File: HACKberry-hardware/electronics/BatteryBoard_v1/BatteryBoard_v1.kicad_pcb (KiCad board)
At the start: 2 copper layers, 8 x 18.1 mm, 0 parts

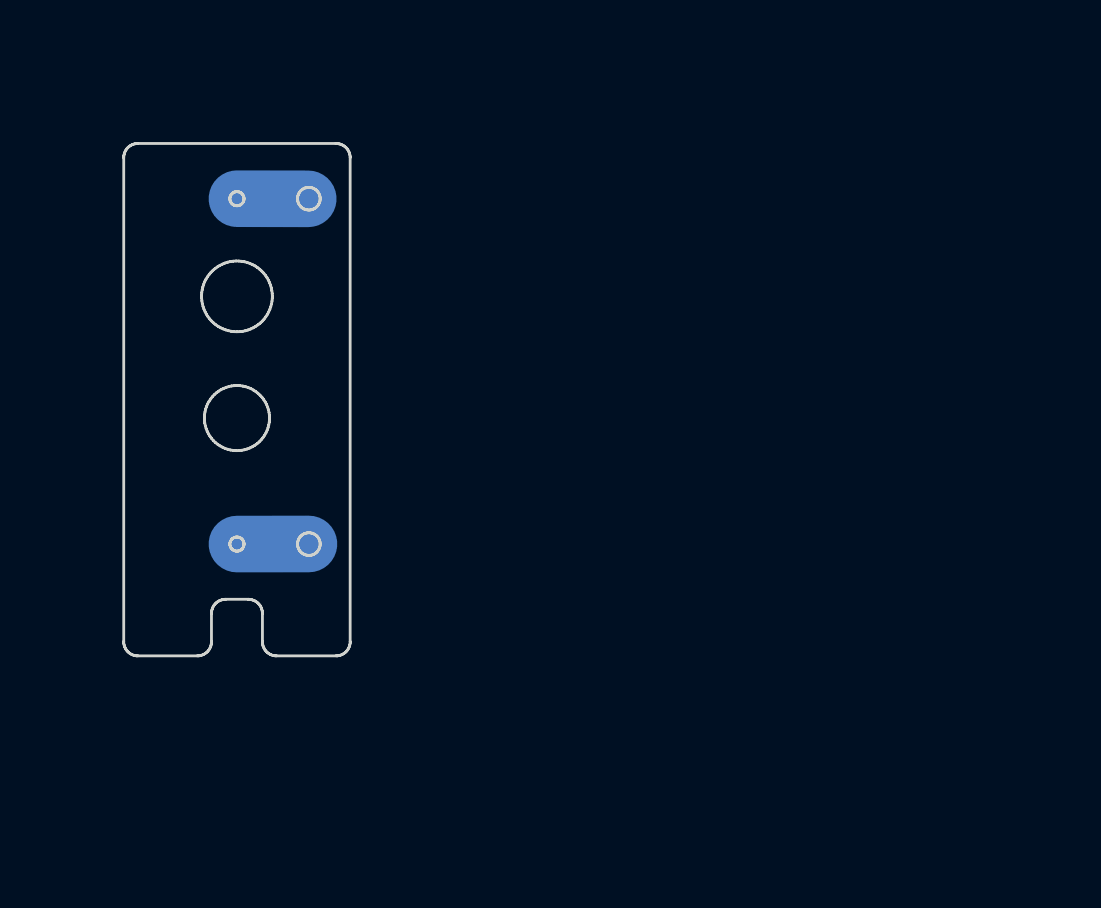
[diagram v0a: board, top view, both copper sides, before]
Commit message: Updated the HandBoard
changed the voltage for sensor from 3.3[V] to 5.0[V].
modified the garber data for milling.
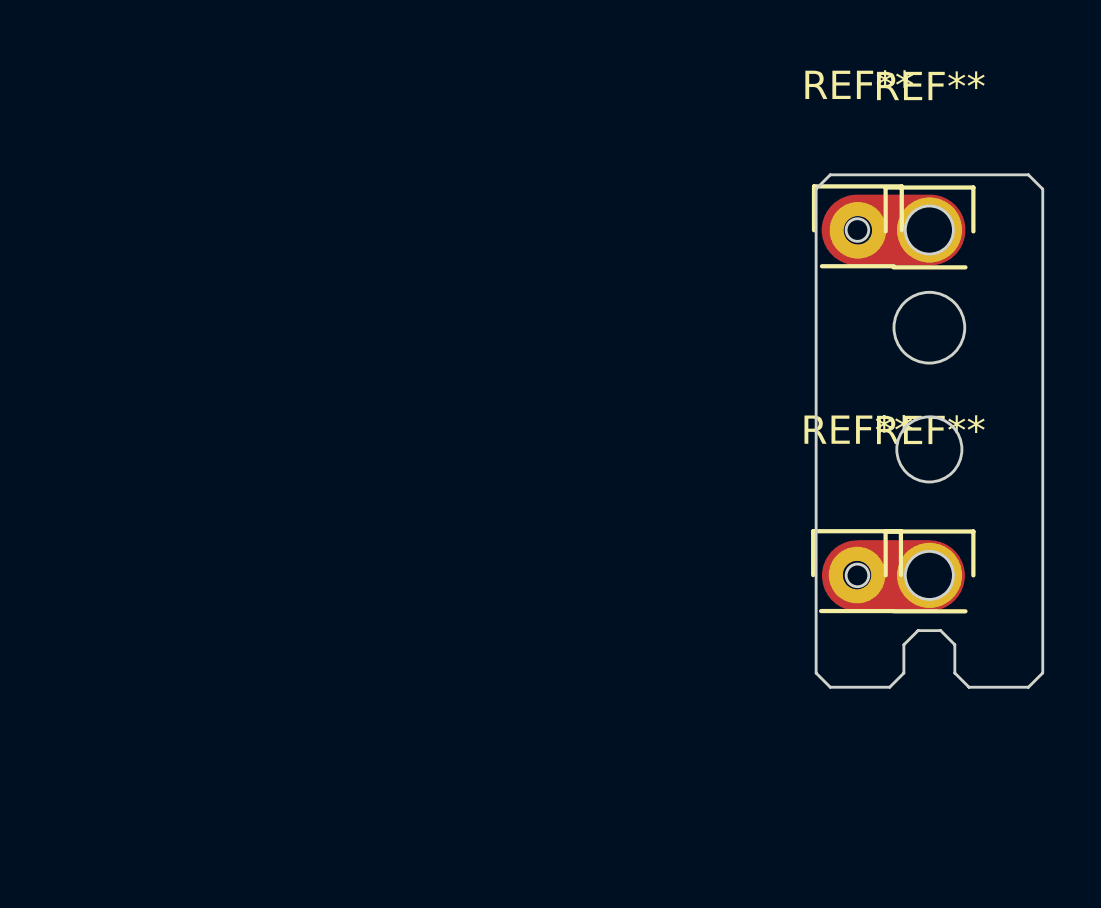
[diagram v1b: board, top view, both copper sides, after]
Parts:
- added REF**: Pin_Header_Straight_1x01, Pin_Headers:Pin_Header_Straight_1x01, F.Cu at (228.2, 136.6)
- added REF**: Pin_Header_Straight_1x01, Pin_Headers:Pin_Header_Straight_1x01, F.Cu at (230.8, 136.7)
- added REF**: Pin_Header_Straight_1x01, Pin_Headers:Pin_Header_Straight_1x01, F.Cu at (228.2, 148.8)
- added REF**: Pin_Header_Straight_1x01, Pin_Headers:Pin_Header_Straight_1x01, F.Cu at (230.8, 148.8)
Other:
- outline, holes or cut-outs redrawn

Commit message: Uploaded the PCB files for manufacturing
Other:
- outline, holes or cut-outs redrawn
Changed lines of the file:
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@@
     (area 218.156713 130.341 240.803287 152.811101)
     (thickness 1.6)
-    (drawings 22)
+    (drawings 20)
     (tracks 4)
     (zones 0)
@@
   (layers
     (0 F.Cu signal)
-    (31 B.Cu signal hide)
-    (32 B.Adhes user hide)
-    (33 F.Adhes user hide)
-    (34 B.Paste user hide)
-    (35 F.Paste user hide)
-    (36 B.SilkS user hide)
-    (37 F.SilkS user hide)
-    (38 B.Mask user hide)
-    (39 F.Mask user hide)
-    (40 Dwgs.User user hide)
-    (41 Cmts.User user hide)
-    (42 Eco1.User user hide)
-    (43 Eco2.User user hide)
+    (31 B.Cu signal)
+    (32 B.Adhes user)
+    (33 F.Adhes user)
+    (34 B.Paste user)
+    (35 F.Paste user)
+    (36 B.SilkS user)
+    (37 F.SilkS user)
+    (38 B.Mask user)
+    (39 F.Mask user)
+    (40 Dwgs.User user)
+    (41 Cmts.User user)
+    (42 Eco1.User user)
+    (43 Eco2.User user)
     (44 Edge.Cuts user)
   )
   (setup
-    (last_trace_width 2.5)
+    (last_trace_width 0.254)
     (user_trace_width 2)
     (user_trace_width 2.5)
@@
     (mod_text_width 0.15)
     (pad_size 2.3 2.3)
-    (pad_drill 1.7)
+    (pad_drill 1.5)
     (pad_to_mask_clearance 0.2)
     (aux_axis_origin 0 0)
@@
       (drillshape 0)
       (scaleselection 1)
-      (outputdirectory 151101BatteryBoard_v1_01/))
+      (outputdirectory 151112BatteryBoard_v1_01/))
   )
   (net 0 "")
@@
     (fp_line (start -1.55 -1.55) (end 1.55 -1.55) (layer F.SilkS) (width 0.15))
     (fp_line (start -1.27 1.27) (end 1.27 1.27) (layer F.SilkS) (width 0.15))
-    (pad 1 thru_hole circle (at 0 -0.05) (size 2.3 2.3) (drill 1.7) (layers *.Cu *.Mask F.SilkS))
+    (pad 1 thru_hole circle (at 0 -0.05) (size 2.3 2.3) (drill 1.5) (layers *.Cu *.Mask F.SilkS))
     (model Pin_Headers.3dshapes/Pin_Header_Straight_1x01.wrl
       (at (xyz 0 0 0))
@@
     (fp_line (start -1.55 -1.55) (end 1.55 -1.55) (layer F.SilkS) (width 0.15))
     (fp_line (start -1.27 1.27) (end 1.27 1.27) (layer F.SilkS) (width 0.15))
-    (pad 1 thru_hole circle (at 0 0) (size 2.3 2.3) (drill 1.7) (layers *.Cu *.Mask F.SilkS))
+    (pad 1 thru_hole circle (at 0 0) (size 2.3 2.3) (drill 1.5) (layers *.Cu *.Mask F.SilkS))
     (model Pin_Headers.3dshapes/Pin_Header_Straight_1x01.wrl
       (at (xyz 0 0 0))
@@
   (gr_circle (center 228.2145 136.6111) (end 228.6145 136.6111) (layer Edge.Cuts) (width 0.1))
   (gr_circle (center 228.2145 148.8111) (end 228.6145 148.8111) (layer Edge.Cuts) (width 0.1))
-  (gr_circle (center 230.7545 136.6111) (end 231.6045 136.6111) (layer Edge.Cuts) (width 0.1))
-  (gr_circle (center 230.7545 148.8111) (end 231.6045 148.8111) (layer Edge.Cuts) (width 0.1))
   (gr_circle (center 230.7545 140.0611) (end 232.0045 140.0611) (layer Edge.Cuts) (width 0.1))
   (gr_circle (center 230.7545 144.3611) (end 231.9045 144.3611) (layer Edge.Cuts) (width 0.1))
@@
   (gr_line (start 234.2545 134.6611) (end 227.2545 134.6611) (layer Edge.Cuts) (width 0.1))
   (gr_line (start 234.7545 135.1611) (end 234.2545 134.6611) (layer Edge.Cuts) (width 0.1))
+  (segment (start 230.78 136.61) (end 230.79 136.62) (width 0.254) (layer F.Cu) (net 0))
+  (segment (start 230.76 148.82) (end 230.77 148.81) (width 0.254) (layer F.Cu) (net 0))
+  (segment (start 228.21 148.82) (end 230.76 148.82) (width 2.5) (layer F.Cu) (net 0))
   (segment (start 228.2 136.61) (end 230.78 136.61) (width 2.5) (layer F.Cu) (net 0))
-  (segment (start 228.21 148.82) (end 230.76 148.82) (width 2.5) (layer F.Cu) (net 0))
-  (segment (start 230.76 148.82) (end 230.77 148.81) (width 0.254) (layer F.Cu) (net 0))
-  (segment (start 230.78 136.61) (end 230.79 136.62) (width 0.254) (layer F.Cu) (net 0))
 )

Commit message: Added SensorBoard_v1_1
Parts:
- ? (x4): renamed from REF**; value Pin_Header_Straight_1x01 -> (none)
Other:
- outline, holes or cut-outs redrawn
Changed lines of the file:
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@@
     (links 0)
     (no_connects 0)
-    (area 218.156713 130.341 240.803287 152.811101)
+    (area 226.170999 130.341 234.810001 152.811101)
     (thickness 1.6)
-    (drawings 20)
-    (tracks 4)
+    (drawings 17)
+    (tracks 8)
     (zones 0)
     (modules 4)
@@
   (page A3)
   (layers
-    (0 F.Cu signal)
+    (0 F.Cu signal hide)
     (31 B.Cu signal)
-    (32 B.Adhes user)
-    (33 F.Adhes user)
-    (34 B.Paste user)
-    (35 F.Paste user)
-    (36 B.SilkS user)
-    (37 F.SilkS user)
-    (38 B.Mask user)
-    (39 F.Mask user)
-    (40 Dwgs.User user)
-    (41 Cmts.User user)
+    (32 B.Adhes user hide)
+    (33 F.Adhes user hide)
+    (34 B.Paste user hide)
+    (35 F.Paste user hide)
+    (36 B.SilkS user hide)
+    (37 F.SilkS user hide)
+    (38 B.Mask user hide)
+    (39 F.Mask user hide)
+    (40 Dwgs.User user hide)
+    (41 Cmts.User user hide)
     (42 Eco1.User user)
-    (43 Eco2.User user)
+    (43 Eco2.User user hide)
     (44 Edge.Cuts user)
   )
   (setup
     (last_trace_width 0.254)
-    (user_trace_width 2)
+    (user_trace_width 1)
     (user_trace_width 2.5)
     (trace_clearance 0.254)
@@
     (visible_elements 7FFFFFFF)
     (pcbplotparams
-      (layerselection 0x01000_00000001)
+      (layerselection 0x01000_80000000)
       (usegerberextensions true)
       (excludeedgelayer true)
@@
       (drillshape 0)
       (scaleselection 1)
-      (outputdirectory 151112BatteryBoard_v1_01/))
+      (outputdirectory 151217BatteryBoard_v1_02/))
   )
   (net 0 "")
@@
     (descr "Through hole pin header")
     (tags "pin header")
-    (fp_text reference REF** (at 0 -5.1) (layer F.SilkS)
-      (effects (font (size 1 1) (thickness 0.15)))
-    )
-    (fp_text value Pin_Header_Straight_1x01 (at 0 -3.1) (layer F.Fab)
-      (effects (font (size 1 1) (thickness 0.15)))
-    )
-    (fp_line (start 1.55 -1.55) (end 1.55 0) (layer F.SilkS) (width 0.15))
-    (fp_line (start -1.75 -1.75) (end -1.75 1.75) (layer F.CrtYd) (width 0.05))
-    (fp_line (start 1.75 -1.75) (end 1.75 1.75) (layer F.CrtYd) (width 0.05))
-    (fp_line (start -1.75 -1.75) (end 1.75 -1.75) (layer F.CrtYd) (width 0.05))
-    (fp_line (start -1.75 1.75) (end 1.75 1.75) (layer F.CrtYd) (width 0.05))
-    (fp_line (start -1.55 0) (end -1.55 -1.55) (layer F.SilkS) (width 0.15))
-    (fp_line (start -1.55 -1.55) (end 1.55 -1.55) (layer F.SilkS) (width 0.15))
-    (fp_line (start -1.27 1.27) (end 1.27 1.27) (layer F.SilkS) (width 0.15))
-    (pad 1 thru_hole circle (at 0 0) (size 2 2) (drill 1) (layers *.Cu *.Mask F.SilkS))
+    (fp_text reference "" (at 0 -5.1) (layer F.SilkS)
+      (effects (font (size 1 1) (thickness 0.15)))
+    )
+    (fp_text value "" (at 0 -3.1) (layer F.Fab)
+      (effects (font (size 1 1) (thickness 0.15)))
+    )
+    (fp_line (start 1.55 -1.55) (end 1.55 0) (layer F.SilkS) (width 0.15))
+    (fp_line (start -1.75 -1.75) (end -1.75 1.75) (layer F.CrtYd) (width 0.05))
+    (fp_line (start 1.75 -1.75) (end 1.75 1.75) (layer F.CrtYd) (width 0.05))
+    (fp_line (start -1.75 -1.75) (end 1.75 -1.75) (layer F.CrtYd) (width 0.05))
+    (fp_line (start -1.75 1.75) (end 1.75 1.75) (layer F.CrtYd) (width 0.05))
+    (fp_line (start -1.55 0) (end -1.55 -1.55) (layer F.SilkS) (width 0.15))
+    (fp_line (start -1.55 -1.55) (end 1.55 -1.55) (layer F.SilkS) (width 0.15))
+    (fp_line (start -1.27 1.27) (end 1.27 1.27) (layer F.SilkS) (width 0.15))
+    (pad 1 thru_hole circle (at 0 0) (size 1.5 1.5) (drill 1) (layers *.Cu *.Mask F.SilkS))
     (model Pin_Headers.3dshapes/Pin_Header_Straight_1x01.wrl
       (at (xyz 0 0 0))
@@
     (descr "Through hole pin header")
     (tags "pin header")
-    (fp_text reference REF** (at 0 -5.1) (layer F.SilkS)
-      (effects (font (size 1 1) (thickness 0.15)))
-    )
-    (fp_text value Pin_Header_Straight_1x01 (at 0 -3.1) (layer F.Fab)
+    (fp_text reference "" (at 0 -5.1) (layer F.SilkS)
+      (effects (font (size 1 1) (thickness 0.15)))
+    )
+    (fp_text value "" (at 0 -3.1) (layer F.Fab)
       (effects (font (size 1 1) (thickness 0.15)))
     )
@@
     (descr "Through hole pin header")
     (tags "pin header")
-    (fp_text reference REF** (at 0 -5.1) (layer F.SilkS)
-      (effects (font (size 1 1) (thickness 0.15)))
-    )
-    (fp_text value Pin_Header_Straight_1x01 (at 0 -3.1) (layer F.Fab)
-      (effects (font (size 1 1) (thickness 0.15)))
-    )
-    (fp_line (start 1.55 -1.55) (end 1.55 0) (layer F.SilkS) (width 0.15))
-    (fp_line (start -1.75 -1.75) (end -1.75 1.75) (layer F.CrtYd) (width 0.05))
-    (fp_line (start 1.75 -1.75) (end 1.75 1.75) (layer F.CrtYd) (width 0.05))
-    (fp_line (start -1.75 -1.75) (end 1.75 -1.75) (layer F.CrtYd) (width 0.05))
-    (fp_line (start -1.75 1.75) (end 1.75 1.75) (layer F.CrtYd) (width 0.05))
-    (fp_line (start -1.55 0) (end -1.55 -1.55) (layer F.SilkS) (width 0.15))
-    (fp_line (start -1.55 -1.55) (end 1.55 -1.55) (layer F.SilkS) (width 0.15))
-    (fp_line (start -1.27 1.27) (end 1.27 1.27) (layer F.SilkS) (width 0.15))
-    (pad 1 thru_hole circle (at 0 0) (size 2 2) (drill 1) (layers *.Cu *.Mask F.SilkS))
+    (fp_text reference "" (at 0 -5.1) (layer F.SilkS)
+      (effects (font (size 1 1) (thickness 0.15)))
+    )
+    (fp_text value "" (at 0 -3.1) (layer F.Fab)
+      (effects (font (size 1 1) (thickness 0.15)))
+    )
+    (fp_line (start 1.55 -1.55) (end 1.55 0) (layer F.SilkS) (width 0.15))
+    (fp_line (start -1.75 -1.75) (end -1.75 1.75) (layer F.CrtYd) (width 0.05))
+    (fp_line (start 1.75 -1.75) (end 1.75 1.75) (layer F.CrtYd) (width 0.05))
+    (fp_line (start -1.75 -1.75) (end 1.75 -1.75) (layer F.CrtYd) (width 0.05))
+    (fp_line (start -1.75 1.75) (end 1.75 1.75) (layer F.CrtYd) (width 0.05))
+    (fp_line (start -1.55 0) (end -1.55 -1.55) (layer F.SilkS) (width 0.15))
+    (fp_line (start -1.55 -1.55) (end 1.55 -1.55) (layer F.SilkS) (width 0.15))
+    (fp_line (start -1.27 1.27) (end 1.27 1.27) (layer F.SilkS) (width 0.15))
+    (pad 1 thru_hole circle (at 0 0) (size 1.5 1.5) (drill 1) (layers *.Cu *.Mask F.SilkS))
     (model Pin_Headers.3dshapes/Pin_Header_Straight_1x01.wrl
       (at (xyz 0 0 0))
@@
     (descr "Through hole pin header")
     (tags "pin header")
-    (fp_text reference REF** (at 0 -5.1) (layer F.SilkS)
-      (effects (font (size 1 1) (thickness 0.15)))
-    )
-    (fp_text value Pin_Header_Straight_1x01 (at 0 -3.1) (layer F.Fab)
+    (fp_text reference "" (at 0 -5.1) (layer F.SilkS)
+      (effects (font (size 1 1) (thickness 0.15)))
+    )
+    (fp_text value "" (at 0 -3.1) (layer F.Fab)
       (effects (font (size 1 1) (thickness 0.15)))
     )
@@
   )
   (gr_line (start 234.76 152.26) (end 234.76 135.16) (angle 90) (layer Edge.Cuts) (width 0.1))
-  (gr_circle (center 228.2145 136.6111) (end 228.6145 136.6111) (layer Edge.Cuts) (width 0.1))
-  (gr_circle (center 228.2145 148.8111) (end 228.6145 148.8111) (layer Edge.Cuts) (width 0.1))
-  (gr_circle (center 230.7545 140.0611) (end 232.0045 140.0611) (layer Edge.Cuts) (width 0.1))
   (gr_circle (center 230.7545 144.3611) (end 231.9045 144.3611) (layer Edge.Cuts) (width 0.1))
   (gr_line (start 234.2545 152.7611) (end 234.7545 152.2611) (layer Edge.Cuts) (width 0.1))
@@
   (segment (start 230.78 136.61) (end 230.79 136.62) (width 0.254) (layer F.Cu) (net 0))
   (segment (start 230.76 148.82) (end 230.77 148.81) (width 0.254) (layer F.Cu) (net 0))
-  (segment (start 228.21 148.82) (end 230.76 148.82) (width 2.5) (layer F.Cu) (net 0))
-  (segment (start 228.2 136.61) (end 230.78 136.61) (width 2.5) (layer F.Cu) (net 0))
+  (segment (start 230.75 136.62) (end 230.76 136.61) (width 2) (layer B.Cu) (net 0))
+  (segment (start 230.75 148.8) (end 230.76 148.81) (width 2) (layer B.Cu) (net 0))
+  (segment (start 230.75 136.62) (end 230.76 136.61) (width 1) (layer B.Cu) (net 0))
+  (segment (start 228.23 136.62) (end 230.75 136.62) (width 1) (layer B.Cu) (net 0))
+  (segment (start 230.75 148.8) (end 230.76 148.81) (width 1) (layer B.Cu) (net 0))
+  (segment (start 228.2 148.8) (end 230.75 148.8) (width 1) (layer B.Cu) (net 0))
 )

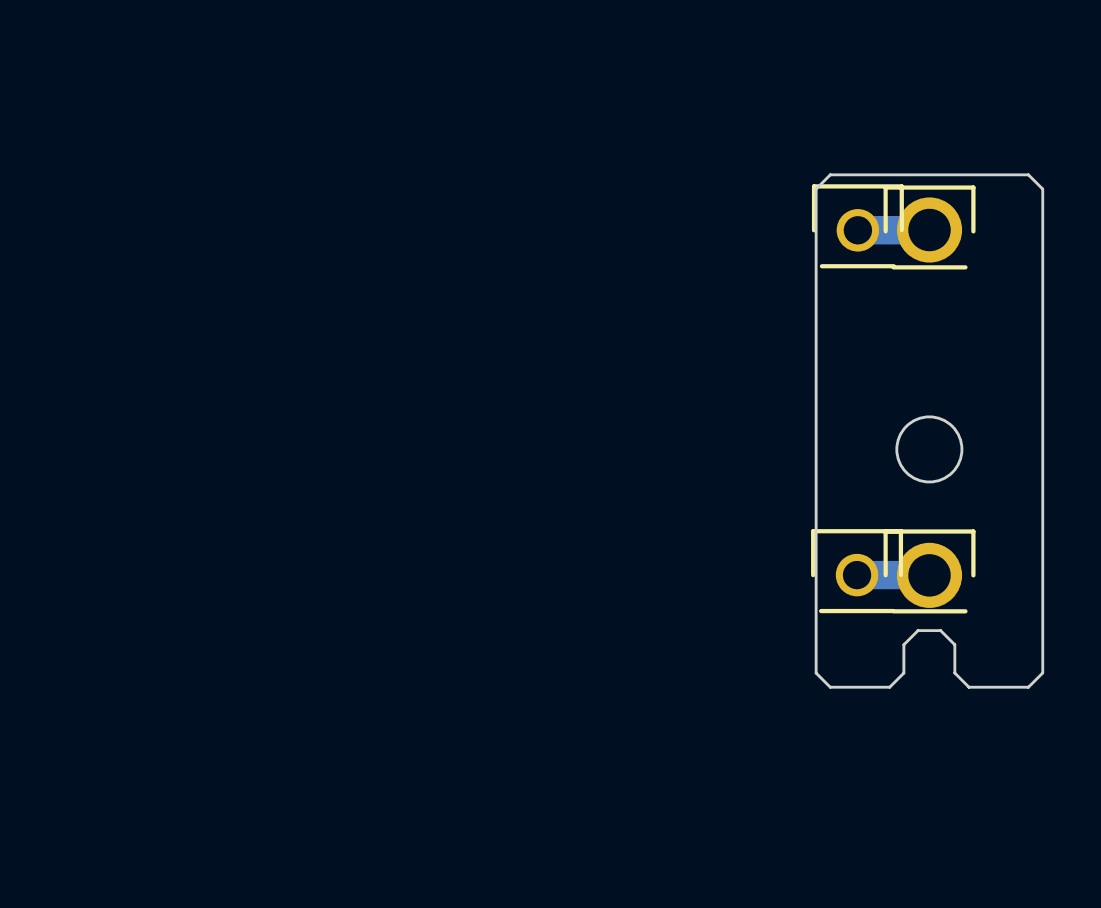
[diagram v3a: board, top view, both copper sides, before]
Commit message: Changed the configuration of battery case
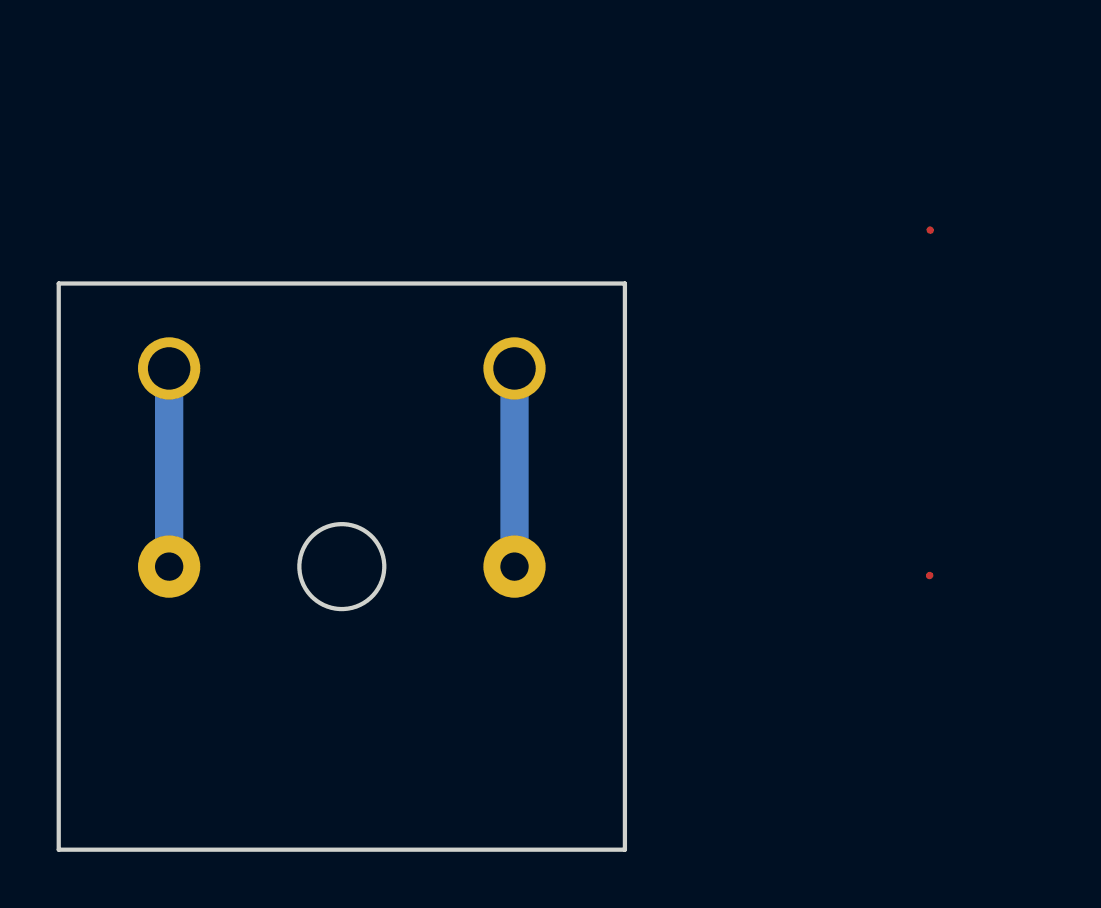
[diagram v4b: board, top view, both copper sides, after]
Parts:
- removed the ? at (228.2, 136.6)
- removed the ? at (230.8, 136.7)
- removed the ? at (228.2, 148.8)
- removed the ? at (230.8, 148.8)
- added ?: , Pin_Headers:Pin_Header_Straight_1x01, F.Cu at (217.3, 147.2)
- added ?: , Pin_Headers:Pin_Header_Straight_1x01, F.Cu at (205.2, 147.2)
- added ?: , Pin_Headers:Pin_Header_Straight_1x01, F.Cu at (217.3, 140.2)
- added ?: , Pin_Headers:Pin_Header_Straight_1x01, F.Cu at (205.2, 140.2)
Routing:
- net (no net): track 5.15 -> 14.0 mm
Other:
- board size 8 x 18.1 mm -> 20 x 20 mm
- board text added: "+"
- board text added: "-"
- board text added: "exiii"

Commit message: Updated the PCB files for PCB manufacturing service.
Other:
- board text added: "BatteryBoard_v1"
- board text removed: "exiii"
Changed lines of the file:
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@@
     (links 0)
     (no_connects 0)
-    (area 226.170999 130.341 234.810001 152.811101)
+    (area 199.924999 133.971 231.171002 158.575001)
     (thickness 1.6)
     (drawings 17)
@@
     (34 B.Paste user hide)
     (35 F.Paste user hide)
-    (36 B.SilkS user hide)
+    (36 B.SilkS user)
     (37 F.SilkS user)
-    (38 B.Mask user hide)
+    (38 B.Mask user)
     (39 F.Mask user)
     (40 Dwgs.User user hide)
@@
   )
   (setup
-    (last_trace_width 1)
+    (last_trace_width 0.254)
     (user_trace_width 1)
     (user_trace_width 2.5)
@@
       (viasonmask false)
       (mode 1)
-      (useauxorigin true)
+      (useauxorigin false)
       (hpglpennumber 1)
       (hpglpenspeed 20)
@@
       (drillshape 0)
       (scaleselection 1)
-      (outputdirectory 151221BatteryBoard_v1_03/))
+      (outputdirectory 160111BatteryBoard_v1_05/))
   )
   (net 0 "")
@@
     )
   )
-  (gr_text exiii (at 215.7 155.8) (layer F.Mask)
-    (effects (font (size 1.5 1.5) (thickness 0.3)))
+  (gr_text BatteryBoard_v1 (at 218.9 156.9) (layer F.Mask)
+    (effects (font (size 1.5 1.5) (thickness 0.3)) (justify right))
   )
   (gr_text - (at 216.1 151.4) (layer F.Mask)
